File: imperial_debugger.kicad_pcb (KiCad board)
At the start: 4 copper layers, 80 x 90 mm, 100 parts, among them J1 Conn_02x06_Odd_Even, J2 Conn_02x06_Odd_Even, J3 Conn_02x06_Odd_Even, J4 Conn_02x06_Odd_Even, J5 USB_C_Receptacle_USB2.0_14P, Q1 SI500N025UK-TP, Q2 SI500N025UK-TP, SW1 ResetButton, U1 TLV75525PDBV, U2 TLV75518PDBV, U3 LM2594M-3.3, U4 FT4232H, U5 93LC54B, Y1 ABLS7M2-12.000MHZ-D2Y-T

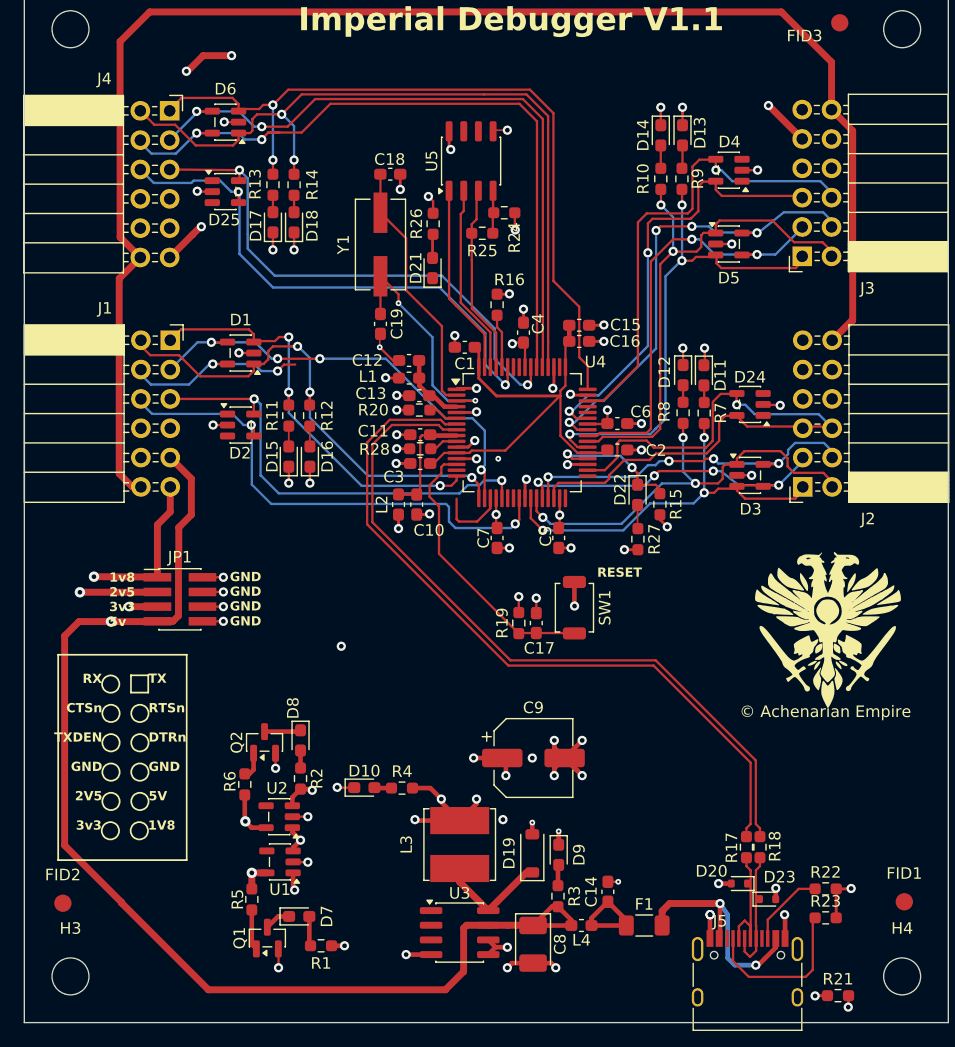
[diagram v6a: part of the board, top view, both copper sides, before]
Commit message: Update schematics after moving to KiCad 10
Added some footprints to a local lib, as the silkscreen caused issues.

Signed-off-by: Marc Kelly <mpkelly@achenar.co.uk>
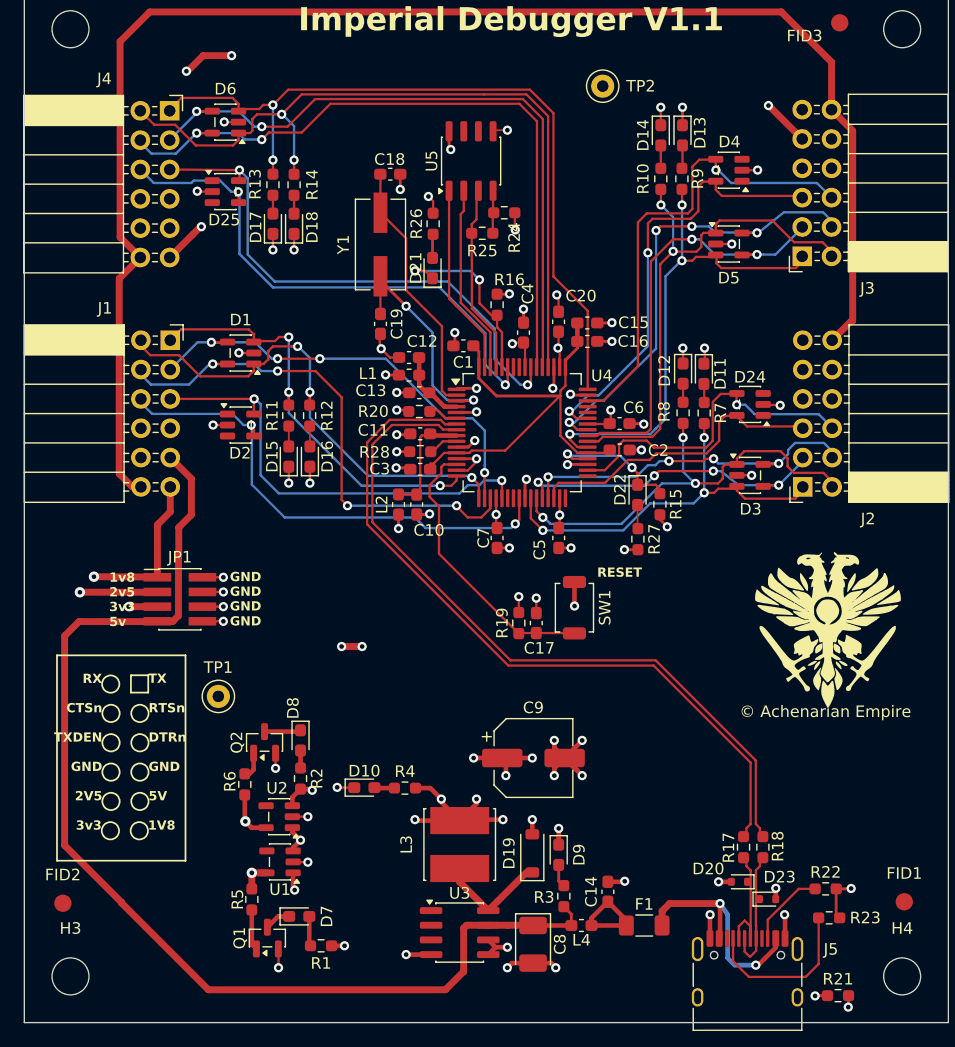
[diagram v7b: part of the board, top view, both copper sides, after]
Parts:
- added C20: 100nF, Capacitor_SMD:C_0603_1608Metric_Pad1.08x0.95mm_HandSolder, F.Cu at (96.3, 79.3)
- added TP1: GND_Connect, TestPoint:TestPoint_Keystone_5000-5004_Miniature, F.Cu at (66.8, 111.8)
- added TP2: GND_Connect, TestPoint:TestPoint_Keystone_5000-5004_Miniature, F.Cu at (100.1, 58.9)
- L3: footprint Inductor_SMD:L_Bourns_SRN6045TA -> Local_FootPrints:L_Bourns_SRN6045TA
- moved C15 0.73 mm to (98.7, 79.4)
- moved C16 0.70 mm to (98.7, 81.0)
- moved R3 0.51 mm to (96.7, 129.1)
- moved C3 0.51 mm to (84.3, 92.1)
- moved R23 0.30 mm to (119.7, 130.9)
- moved C12 0.25 mm to (83.3, 82.4)
- moved R17 0.25 mm to (112.3, 124.8)
- moved R18 0.25 mm to (113.9, 124.8)
- moved R28 0.25 mm to (84.3, 90.6)
- moved R4 0.25 mm to (83.0, 119.7)
- moved C13 0.25 mm to (84.2, 85.5)
- moved L1 0.25 mm to (83.3, 83.9)
- moved C2 0.20 mm to (101.5, 90.4)
- moved C6 0.19 mm to (101.5, 88.1)
- moved C1 0.18 mm to (88.0, 81.4)
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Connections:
- J5 pad A8: unconnected-(J5-SBU1-PadA8) -> (no net)
- J5 pad B8: unconnected-(J5-SBU2-PadB8) -> (no net)
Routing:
- net ADBUS3: track 22.8 -> 45.0 mm, vias 2 -> 4
- net PWREN#: track 4.66 -> 16.3 mm, vias 0 -> 2
- net +3V3: track 215.9 -> 227.3 mm, vias 27 -> 29
- net GND: track 106.9 -> 111.7 mm
- net VBUS: track 221.5 -> 218.5 mm, vias 4 -> 3
- net BDBUS4: track 28.6 -> 26.5 mm
- net BDBUS2: track 29.7 -> 28.0 mm
- net DDBUS3: track 61.0 -> 60.1 mm
- net /USB and Power/VREGOUT: track 38.9 -> 39.6 mm
- net ADBUS7: track 44.5 -> 43.8 mm
- net /USB and Power/RESET#: vias 1 -> 0

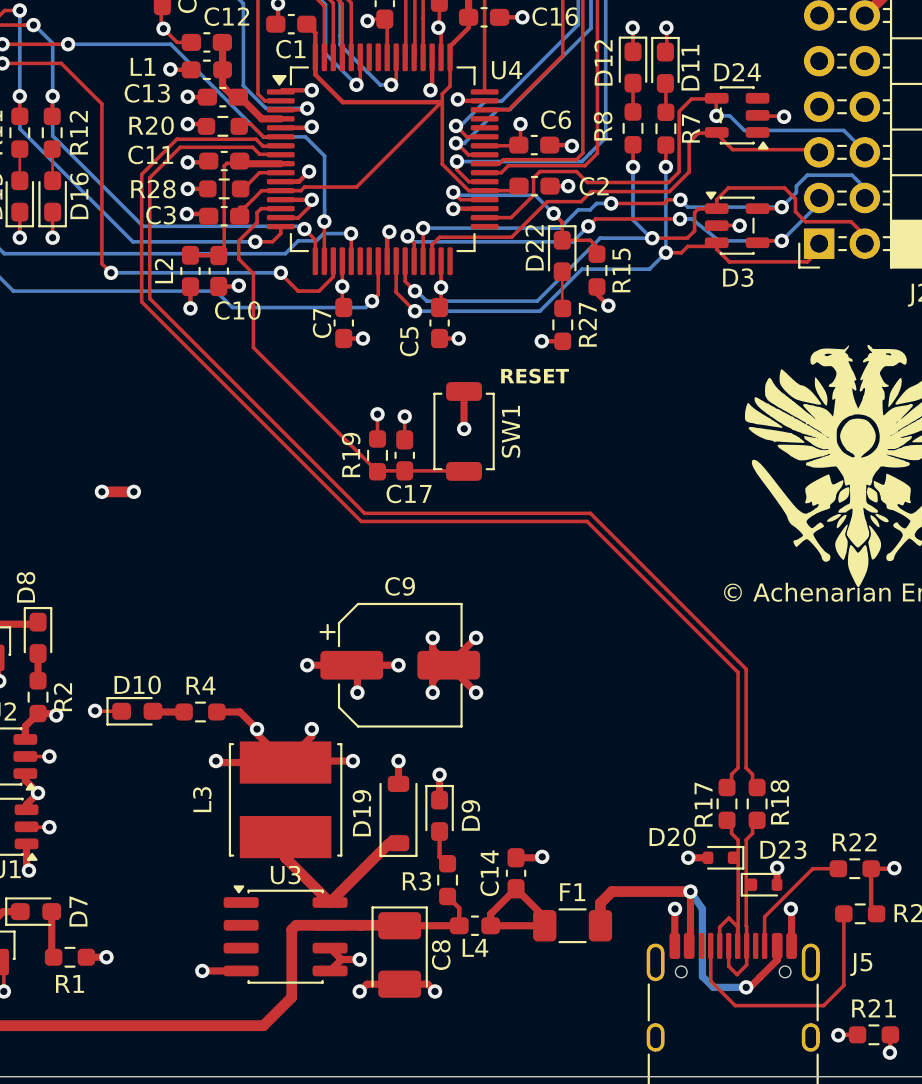
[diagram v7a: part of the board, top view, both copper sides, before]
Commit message: Update USB routing
Signed-off-by: Marc Kelly <mpkelly@achenar.co.uk>
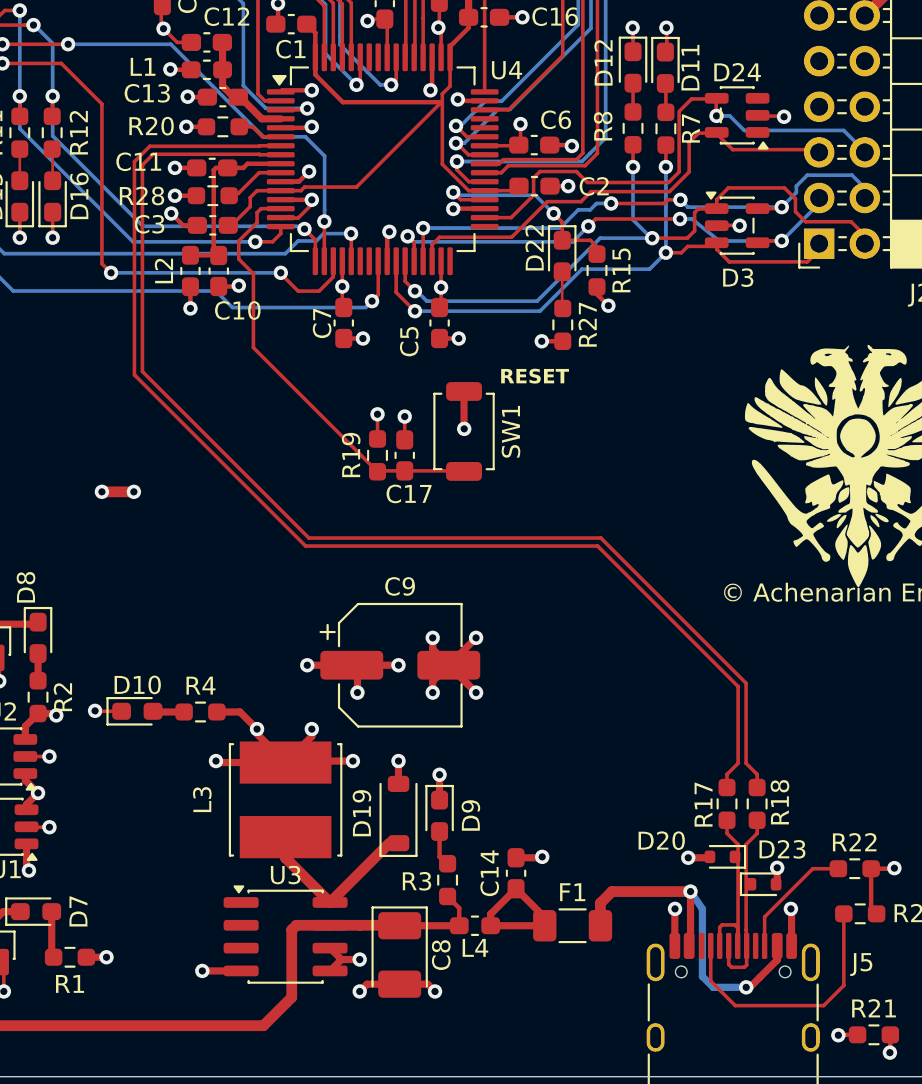
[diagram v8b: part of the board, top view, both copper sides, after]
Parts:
- moved C3 0.81 mm to (83.6, 92.6)
- moved C11 0.77 mm to (83.6, 89.4)
- moved R28 0.74 mm to (83.6, 91.0)
- moved D20 0.11 mm to (112.0, 127.8)
- moved D23 0.06 mm to (114.3, 129.3)
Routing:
- net /USB and Power/D_P: track 63.4 -> 67.0 mm
- net /USB and Power/D_N: track 64.1 -> 67.7 mm
- net /USB and Power/VREGOUT: track 39.6 -> 40.6 mm
- net VPLL: track 10.0 -> 10.8 mm
- net GND: track 111.7 -> 112.3 mm
- net Net-(U4-AGND): track 2.50 -> 3.10 mm
